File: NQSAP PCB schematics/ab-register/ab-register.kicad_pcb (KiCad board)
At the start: 2 copper layers, 102 x 96 mm, 56 parts, among them J1 Bus, J2 Bus, J5 Conn_02x08, J6 Conn_02x08, U1 74LS377, U2 74LS245, U3 74LS377, U4 74LS245, U5 74LS138, U6 74LS138

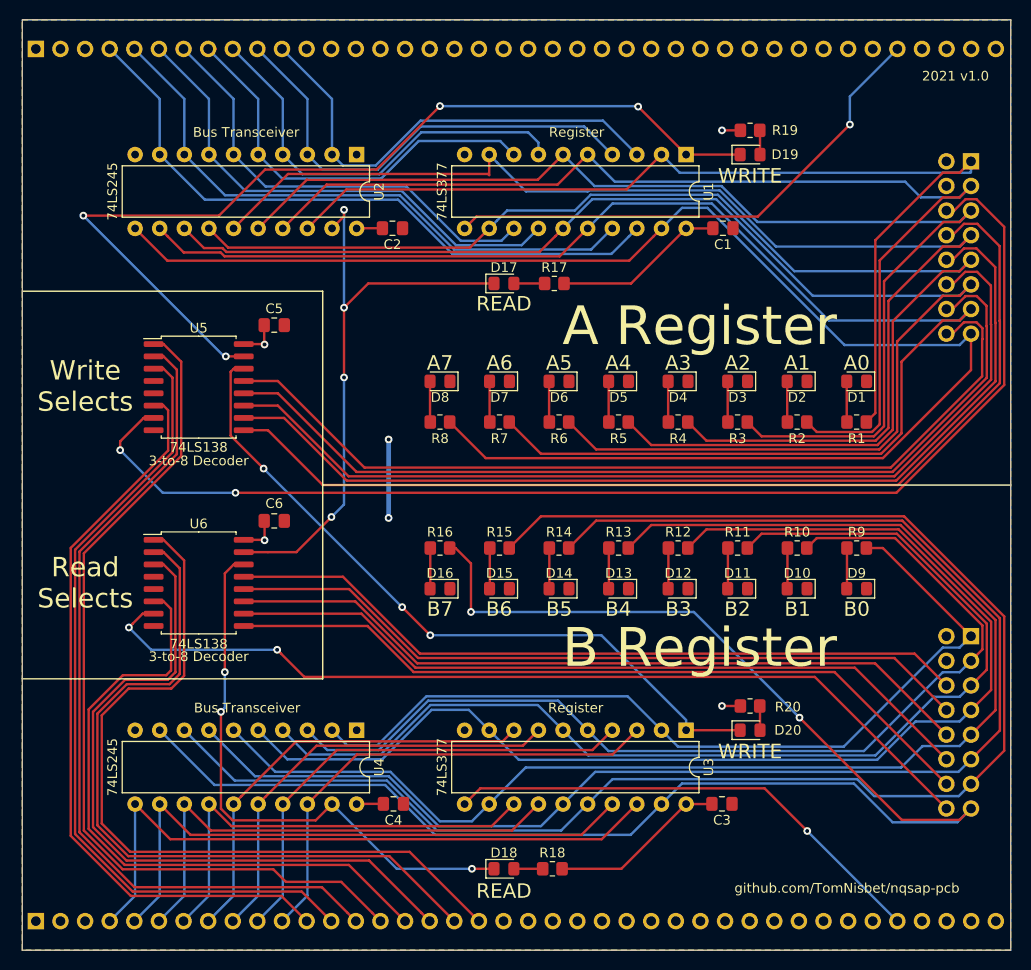
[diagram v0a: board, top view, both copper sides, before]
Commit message: Add RAM, update and add gerbers for new boards
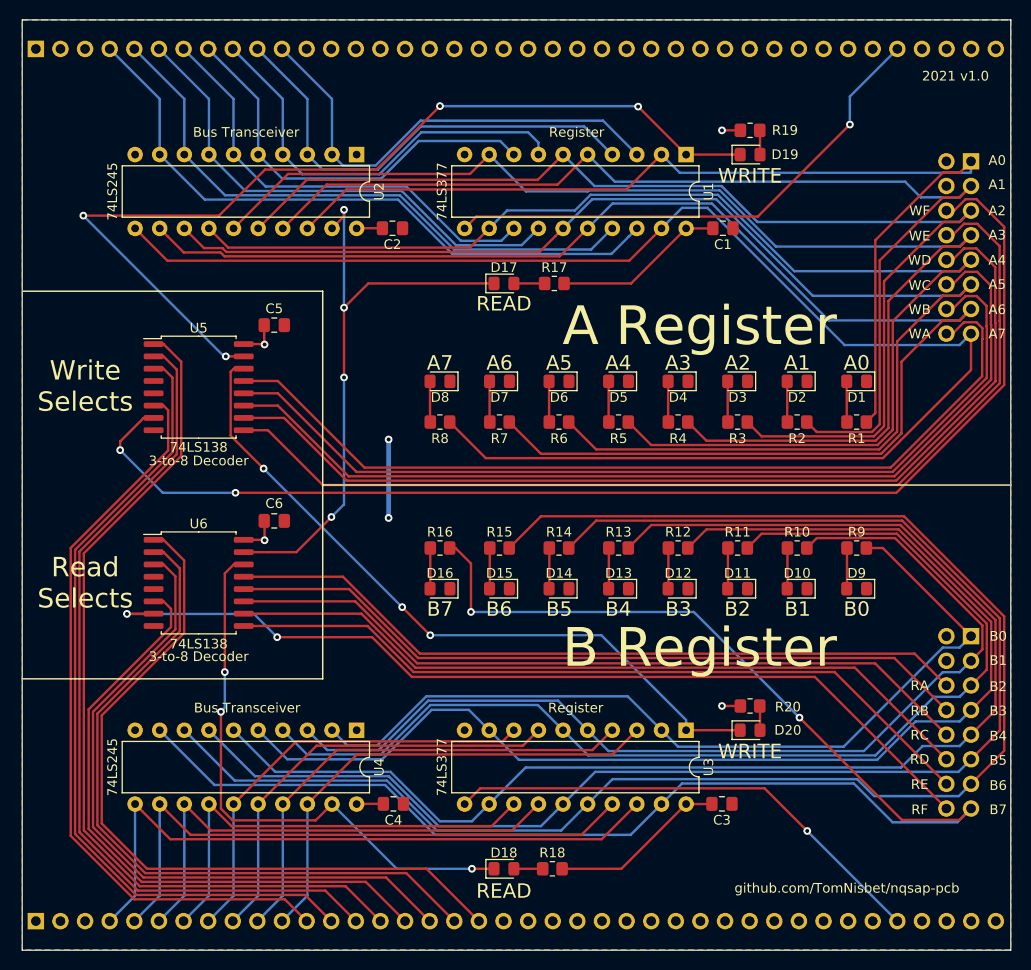
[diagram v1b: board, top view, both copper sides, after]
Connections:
- net ~RF renamed ~RXF
- net ~RH renamed ~RXB
- net ~RL renamed ~RXA
- net ~RP renamed ~RXC
- net ~WI renamed ~WXF
- net ~WO renamed ~WXA
- net ~WP renamed ~WXC
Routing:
- net RR3: track 67.6 -> 64.9 mm
- net RR0: track 80.4 -> 77.8 mm
- net RR2: track 73.5 -> 70.9 mm
- net RR1: track 76.9 -> 74.4 mm
- net /A3: track 131.6 -> 130.3 mm
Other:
- board text added: "A0"
- board text added: "A1"
- board text added: "A2"
- board text added: "A3"
- board text added: "A4"
- board text added: "A5"
- board text added: "A6"
- board text added: "A7"
- board text added: "B0"
- board text added: "B1"
- board text added: "B2"
- board text added: "B3"
- board text added: "B4"
- board text added: "B5"
- board text added: "B6"
- board text added: "B7"
- board text added: "RA"
- board text added: "RB"
- board text added: "RC"
- board text added: "RD"
- board text added: "RE"
- board text added: "RF"
- board text added: "WA"
- board text added: "WB"
- board text added: "WC"
- board text added: "WD"
- board text added: "WE"
- board text added: "WF"

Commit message: updated KiCads and gerbers for the AB Registers and IR/RC module
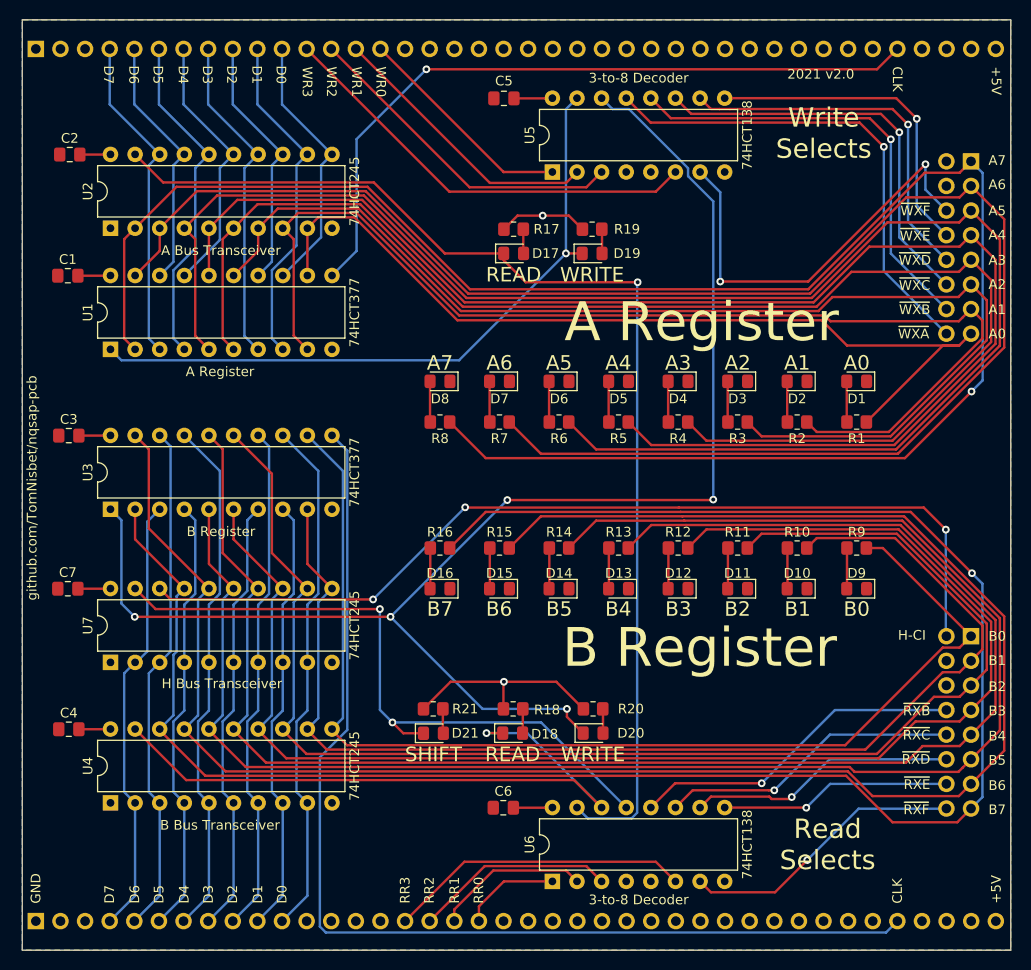
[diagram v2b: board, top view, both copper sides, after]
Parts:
- added C7: 0.1uF, Capacitor_SMD:C_0805_2012Metric_Pad1.18x1.45mm_HandSolder, F.Cu at (89.7, 101.7)
- added D21: SHIFT, LED_SMD:LED_0805_2012Metric_Pad1.15x1.40mm_HandSolder, F.Cu at (127.4, 116.6)
- added R21: R-GN, Resistor_SMD:R_0805_2012Metric_Pad1.20x1.40mm_HandSolder, F.Cu at (127.4, 114.1)
- added U7: 74HCT245, Package_DIP:DIP-20_W7.62mm, F.Cu at (94.1, 109.3)
- U1, U3: value 74LS377 -> 74HCT377
- U2, U4: value 74LS245 -> 74HCT245
- U5, U6: value 74LS138 -> 74HCT138; footprint Package_SO:SOIC-16W_7.5x10.3mm_P1.27mm -> Package_DIP:DIP-16_W7.62mm
- moved C3 77.4 mm to (89.8, 85.9), turned to 0 degrees
- moved C1 67.8 mm to (89.7, 69.4), turned to 0 degrees
- moved U3 63.6 mm to (94.1, 93.5), turned to 90 degrees
- moved U1 62.7 mm to (94.1, 77.0), turned to 90 degrees
- moved U6 47.8 mm to (139.7, 131.9), turned to 90 degrees
- moved U5 42.7 mm to (139.7, 58.7), turned to 90 degrees
- moved C6 37.9 mm to (134.6, 124.3), turned to 0 degrees
- moved C4 34.4 mm to (89.8, 116.2), turned to 0 degrees
- moved C2 34.2 mm to (89.9, 56.9), turned to 0 degrees
- moved C5 33.3 mm to (134.7, 51.1), turned to 0 degrees
- moved U2 26.5 mm to (94.1, 64.5), turned to 90 degrees
- moved U4 26.5 mm to (94.1, 123.8), turned to 90 degrees
- moved D19 19.2 mm to (143.8, 67.1)
- moved R19 19.2 mm to (143.8, 64.6)
- moved R18 17.0 mm to (135.7, 114.1)
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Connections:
- J1 pad 12: Net-(J1-Pad12) -> WR3
- J1 pad 13: Net-(J1-Pad13) -> WR2
- J1 pad 14: Net-(J1-Pad14) -> WR1
- J1 pad 15: Net-(J1-Pad15) -> WR0
- J2 pad 12: WR3 -> Net-(J2-Pad12)
- J2 pad 13: WR2 -> Net-(J2-Pad13)
- J2 pad 14: WR1 -> Net-(J2-Pad14)
- J2 pad 15: WR0 -> Net-(J2-Pad15)
- J5 pad 1: /A0 -> /A7
- J5 pad 11: /A5 -> /A2
- J5 pad 13: /A6 -> /A1
- J5 pad 15: /A7 -> /A0
- J5 pad 3: /A1 -> /A6
- J5 pad 5: /A2 -> /A5
- J5 pad 7: /A3 -> /A4
- J5 pad 9: /A4 -> /A3
- J6 pad 2: Net-(J6-Pad2) -> H-CIN
- J6 pad 6: ~RXA -> Net-(J6-Pad6)
- R17 pad 1: Net-(D17-Pad2) -> +5V
- R17 pad 2: +5V -> Net-(D17-Pad2)
- R18 pad 1: Net-(D18-Pad2) -> +5V
- R18 pad 2: +5V -> Net-(D18-Pad2)
- R20 pad 1: Net-(D20-Pad2) -> +5V
- R20 pad 2: +5V -> Net-(D20-Pad2)
- U1 pad 12: /A4 -> /A0
- U1 pad 13: D4 -> D0
- U1 pad 14: D5 -> D2
- U1 pad 15: /A5 -> /A2
- U1 pad 16: /A6 -> /A4
- U1 pad 17: D6 -> D4
- U1 pad 18: D7 -> D6
- U1 pad 19: /A7 -> /A6
- U1 pad 2: /A0 -> /A7
- U1 pad 3: D0 -> D7
- U1 pad 4: D1 -> D5
- U1 pad 5: /A1 -> /A5
- U1 pad 6: /A2 -> /A3
- U1 pad 7: D2 -> D3
- U1 pad 8: D3 -> D1
- U1 pad 9: /A3 -> /A1
- U2 pad 1: GND -> +5V
- U2 pad 11: /A7 -> D0
- U2 pad 12: /A6 -> D1
- U2 pad 13: /A5 -> D2
- U2 pad 14: /A4 -> D3
- U2 pad 15: /A3 -> D4
- U2 pad 16: /A2 -> D5
- U2 pad 17: /A1 -> D6
- U2 pad 18: /A0 -> D7
- U2 pad 2: D0 -> /A7
- U2 pad 3: D1 -> /A6
- U2 pad 4: D2 -> /A5
- U2 pad 5: D3 -> /A4
- U2 pad 6: D4 -> /A3
- U2 pad 7: D5 -> /A2
- U2 pad 8: D6 -> /A1
- U2 pad 9: D7 -> /A0
- U3 pad 12: /B4 -> /B0
- U3 pad 13: D4 -> D0
- U3 pad 14: D5 -> D2
- U3 pad 15: /B5 -> /B2
- U3 pad 16: /B6 -> /B4
- U3 pad 17: D6 -> D4
- U3 pad 18: D7 -> D6
- U3 pad 19: /B7 -> /B6
- U3 pad 2: /B0 -> /B7
- U3 pad 3: D0 -> D7
- U3 pad 4: D1 -> D5
- U3 pad 5: /B1 -> /B5
- U3 pad 6: /B2 -> /B3
- U3 pad 7: D2 -> D3
- U3 pad 8: D3 -> D1
- U3 pad 9: /B3 -> /B1
- U4 pad 1: +5V -> GND
- U4 pad 11: D7 -> /B0
- U4 pad 12: D6 -> /B1
- U4 pad 13: D5 -> /B2
- U4 pad 14: D4 -> /B3
- U4 pad 15: D3 -> /B4
- U4 pad 16: D2 -> /B5
- U4 pad 17: D1 -> /B6
- U4 pad 18: D0 -> /B7
- U4 pad 2: /B0 -> D7
- U4 pad 3: /B1 -> D6
- U4 pad 4: /B2 -> D5
- U4 pad 5: /B3 -> D4
- U4 pad 6: /B4 -> D3
- U4 pad 7: /B5 -> D2
- U4 pad 8: /B6 -> D1
- U4 pad 9: /B7 -> D0
- U6 pad 13: ~RXA -> ~RH
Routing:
- net H-CIN: track 0.00 -> 97.7 mm, vias 0 -> 3
- net ~WXF: track 127.0 -> 44.0 mm
- net CLK: track 105.0 -> 187.6 mm, vias 2 -> 1
- net ~RXA: track 77.2 -> 0.00 mm
- net ~WB: track 73.8 -> 149.4 mm, vias 3 -> 5
- net ~WXE: track 105.8 -> 34.0 mm, vias 0 -> 1
- net ~RH: track 0.00 -> 69.8 mm, vias 0 -> 2
- net RR0: track 77.8 -> 10.2 mm
- net WR0: track 90.6 -> 23.0 mm
- net ~RXF: track 95.3 -> 29.5 mm, vias 2 -> 1
- net ~WXD: track 102.6 -> 38.2 mm, vias 0 -> 1
- net RR1: track 74.4 -> 16.0 mm
- net WR1: track 87.2 -> 29.0 mm
- net ~RA: track 61.7 -> 119.4 mm, vias 4 -> 1
- net ~WXC: track 99.7 -> 42.3 mm, vias 0 -> 1
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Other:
- board text added: "+5V"
- board text added: "2021 v2.0"
- board text added: "CLK"
- board text added: "D0"
- board text added: "D1"
- board text added: "D2"
- board text added: "D3"
- board text added: "D4"
- board text added: "D5"
- board text added: "D6"
- board text added: "D7"
- board text added: "GND"
- board text added: "H-CI"
- board text added: "RR0"
- board text added: "RR1"
- board text added: "RR2"
- board text added: "RR3"
- board text added: "WR0"
- board text added: "WR1"
- board text added: "WR2"
- board text added: "WR3"
- board text added: "~RXB"
- board text added: "~RXC"
- board text added: "~RXD"
- board text added: "~RXE"
- board text added: "~RXF"
- board text added: "~WXA"
- board text added: "~WXB"
- board text added: "~WXC"
- board text added: "~WXD"
- board text added: "~WXE"
- board text added: "~WXF"
- board text removed: "2021 v1.0"
- board text removed: "RA"
- board text removed: "RB"
- board text removed: "RC"
- board text removed: "RD"
- board text removed: "RE"
- board text removed: "RF"
- board text removed: "WA"
- board text removed: "WB"
- board text removed: "WC"
- board text removed: "WD"
- board text removed: "WE"
- board text removed: "WF"
